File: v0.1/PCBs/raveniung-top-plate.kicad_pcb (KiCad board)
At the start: 2 copper layers, 287 x 111.7 mm, 11 parts

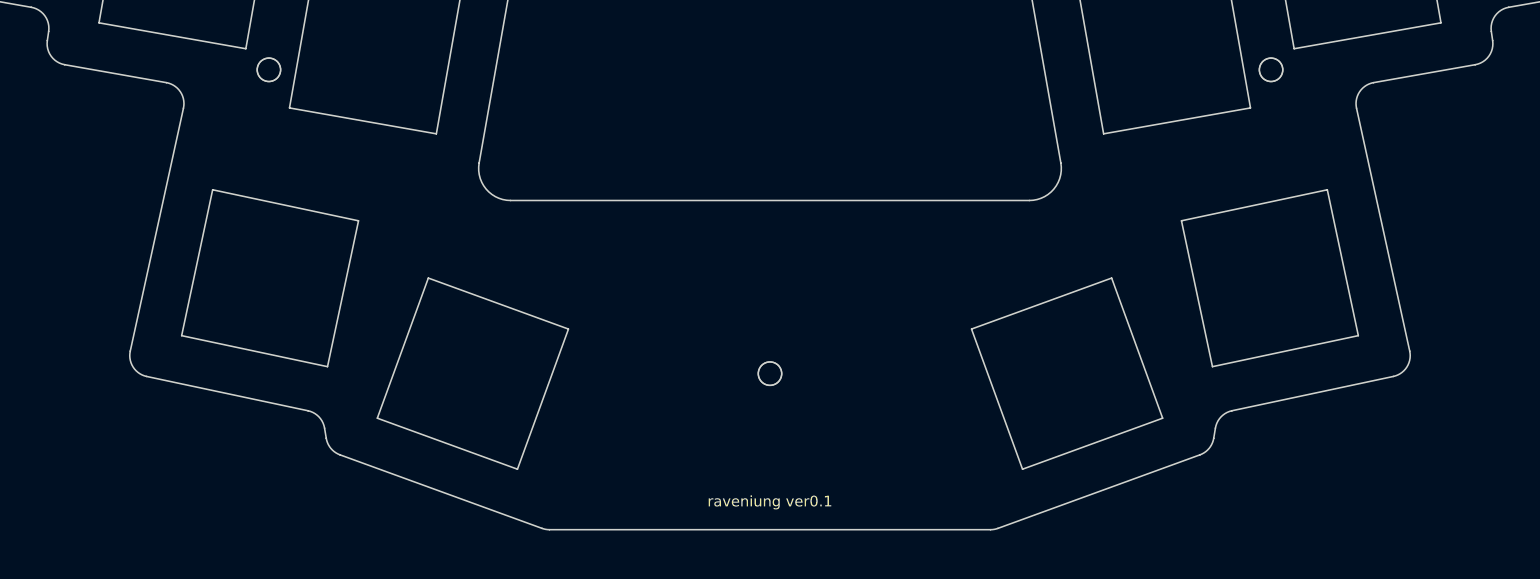
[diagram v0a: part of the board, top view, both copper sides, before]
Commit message: add routed v0.1 PCBs
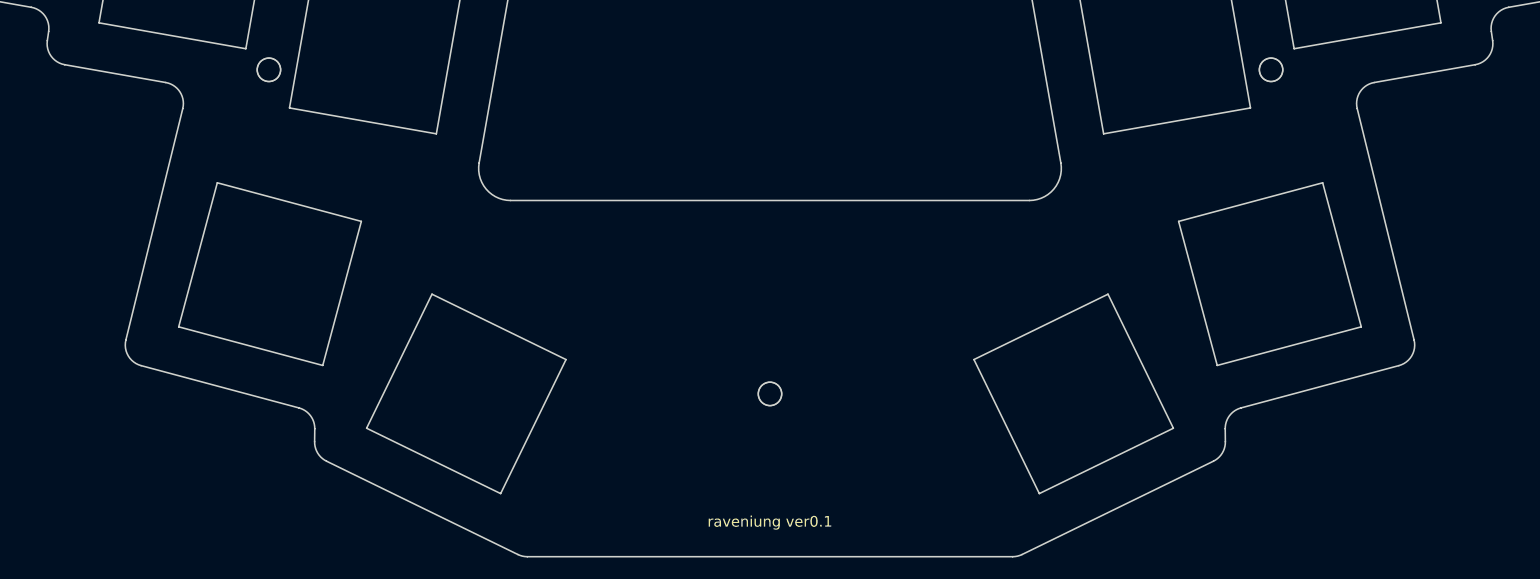
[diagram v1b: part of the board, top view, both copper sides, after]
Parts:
- moved MH1 1.90 mm to (211.7, 164.9)
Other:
- board size 287 x 111.7 mm -> 287 x 114.2 mm
